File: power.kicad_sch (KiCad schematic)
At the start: 40 parts, among them Q1 DMN3008SFG, Q2 DMN3008SFG, U1 AP33771, U2 AP62150WU, U4 AP62150WU, U5 USBLC6-2SC6

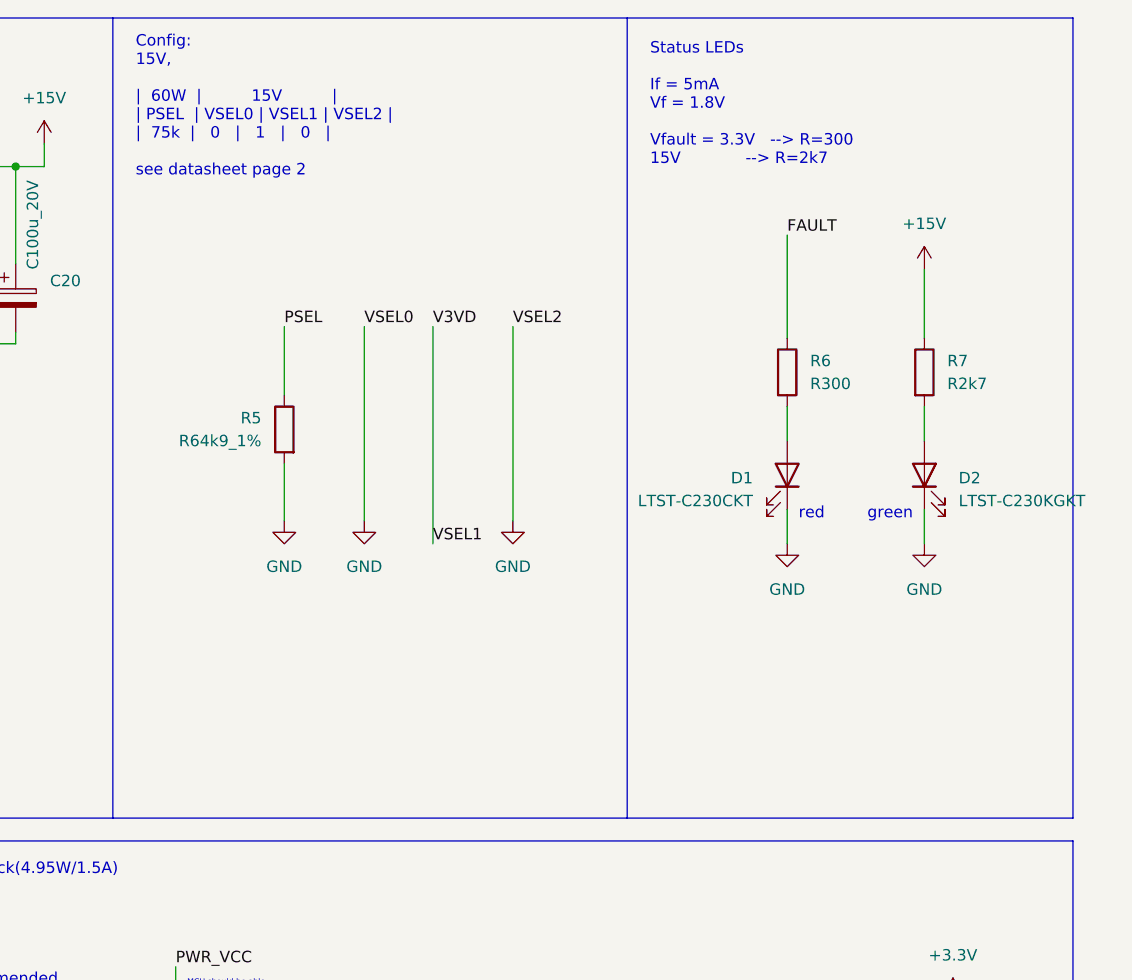
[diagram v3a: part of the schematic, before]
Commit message: Finalize pin mapping, cleanup and layout
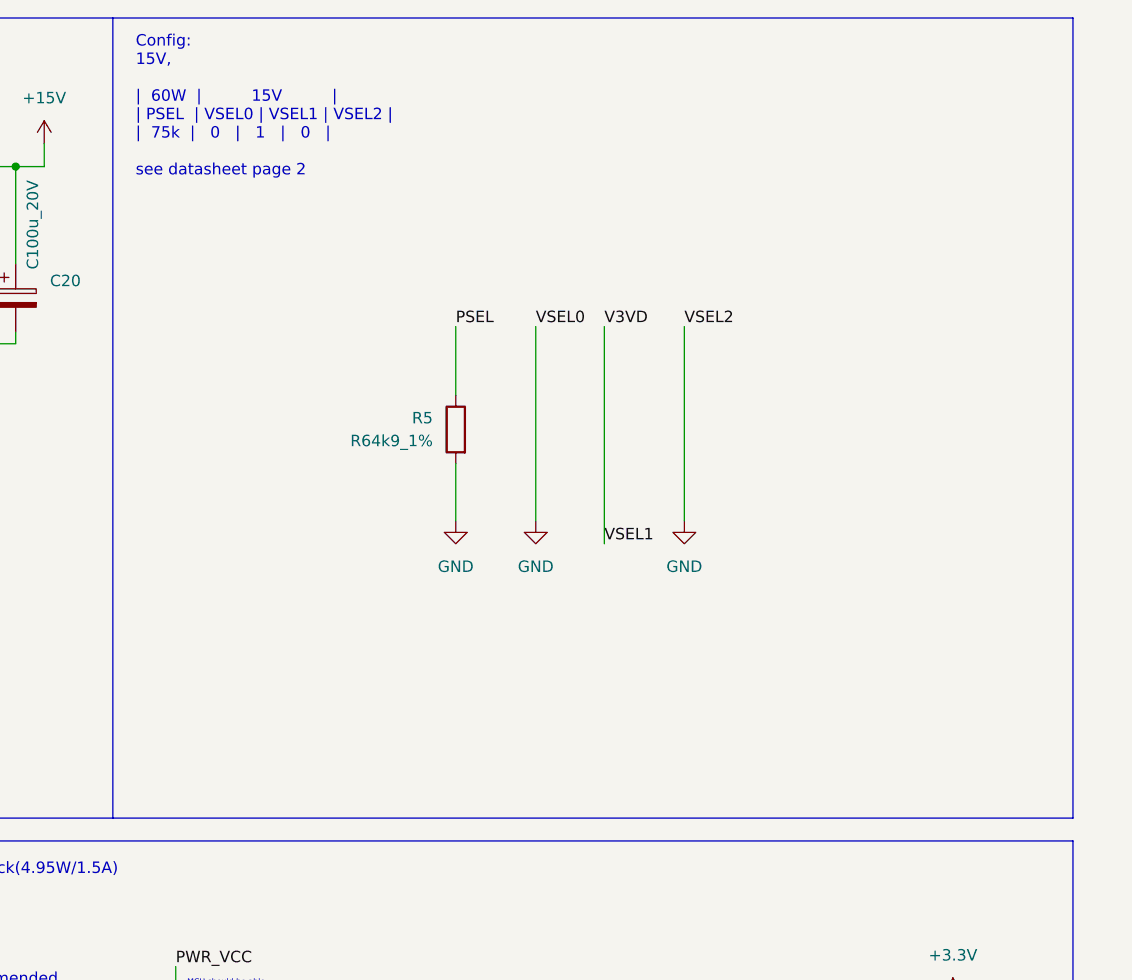
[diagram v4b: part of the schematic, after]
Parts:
- removed D1: LTST-C230CKT, project:LTST-C230, symbol Device:LED
- removed D2: LTST-C230KGKT, project:LTST-C230, symbol Device:LED
- removed R6: R300, Resistor_SMD:R_0805_2012Metric, symbol Device:R
- removed R7: R2k7, Resistor_SMD:R_0805_2012Metric, symbol Device:R
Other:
- note removed: "Status LEDs If = 5mA Vf = 1.8V Vfault = 3.3V --> R=300 15V --> R=2k7"
- note removed: "green"
- note removed: "red"
- moved on the sheet: R5

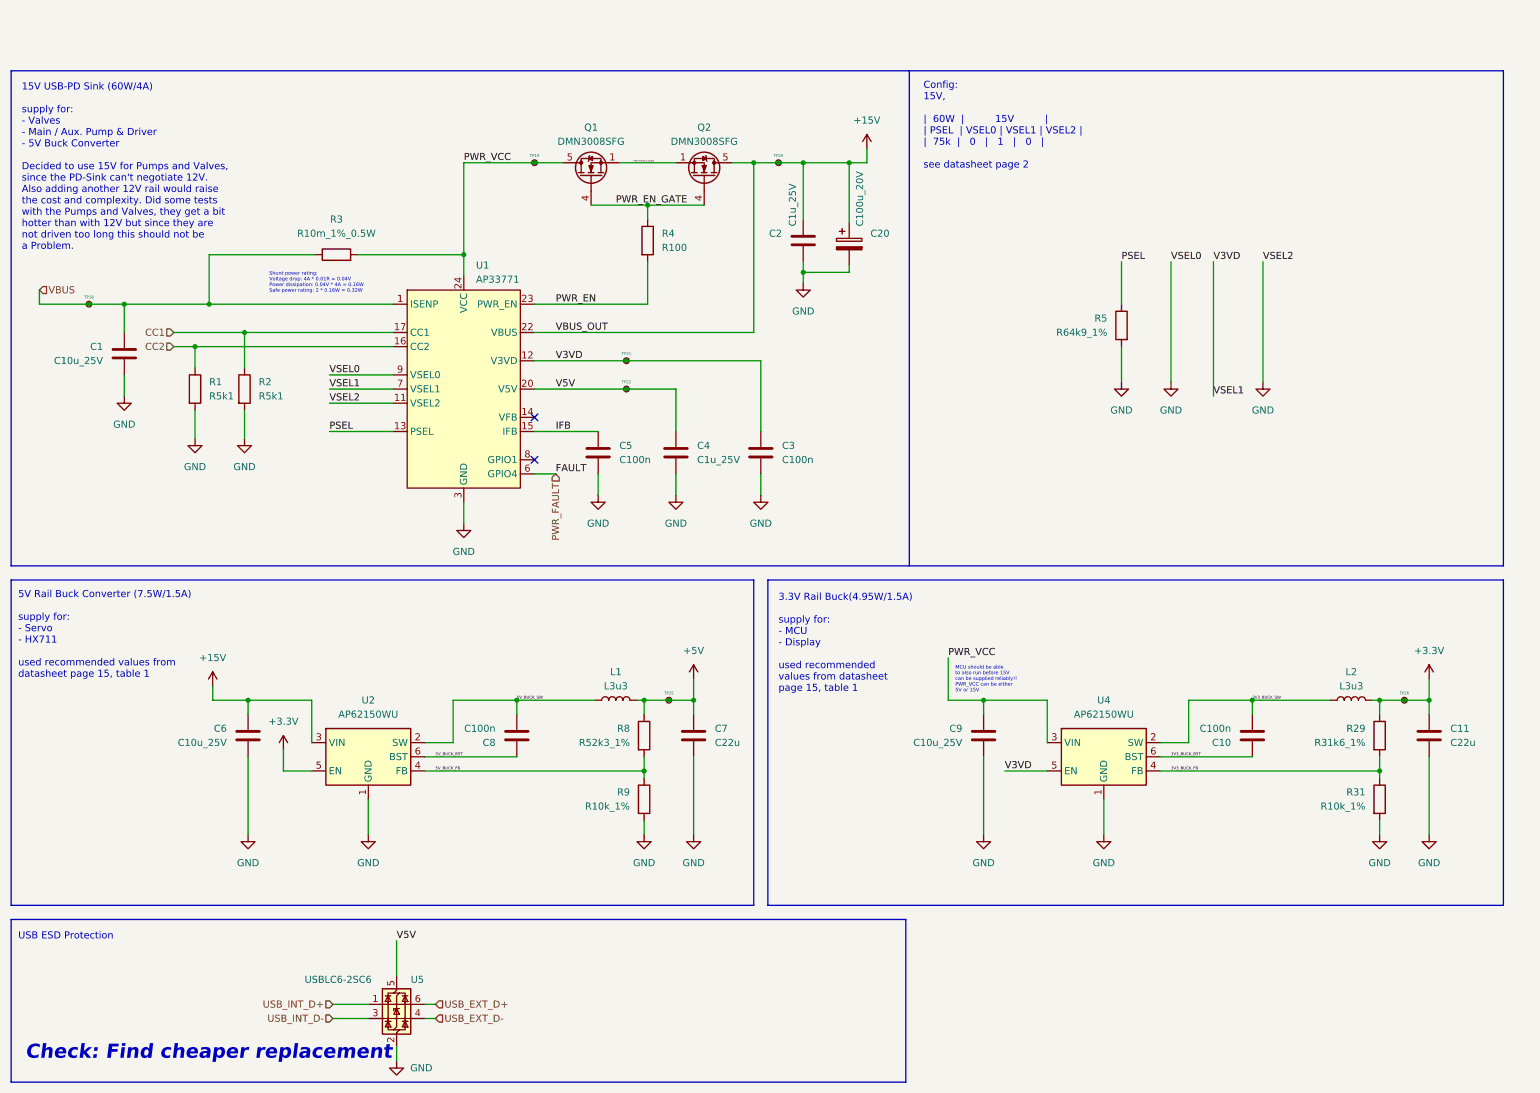
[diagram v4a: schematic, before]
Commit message: Re-annotate parts by board
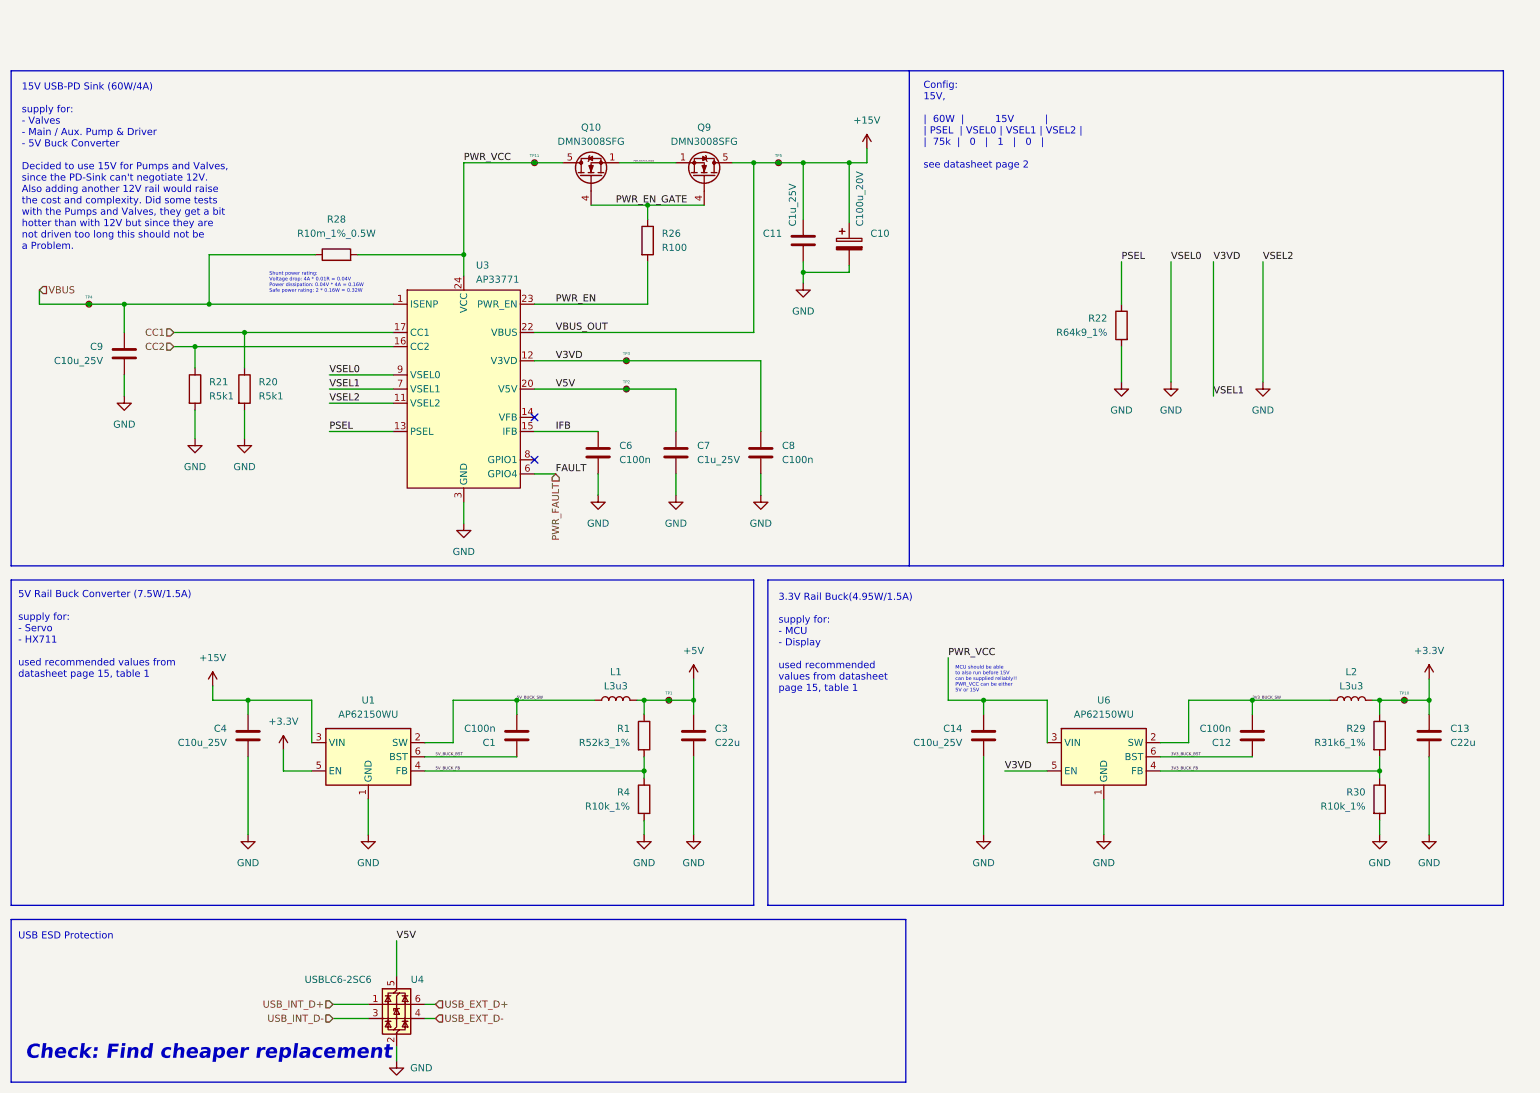
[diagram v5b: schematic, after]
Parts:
- renumbered C8 to C1, C20 to C10, C2 to C11, C10 to C12, C11 to C13, C9 to C14, C7 to C3, C6 to C4, C5 to C6, C4 to C7, C3 to C8, C1 to C9, Q1 to Q10, Q2 to Q9, R8 to R1, R2 to R20, R1 to R21, R5 to R22, R4 to R26, R3 to R28, R31 to R30, R9 to R4, TP25 to TP1, TP26 to TP10, TP19 to TP11, TP22 to TP2, TP21 to TP3, TP18 to TP4, TP20 to TP5, U2 to U1, U1 to U3, U5 to U4, U4 to U6

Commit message: Redesign power rails to use barrel jack 12V input
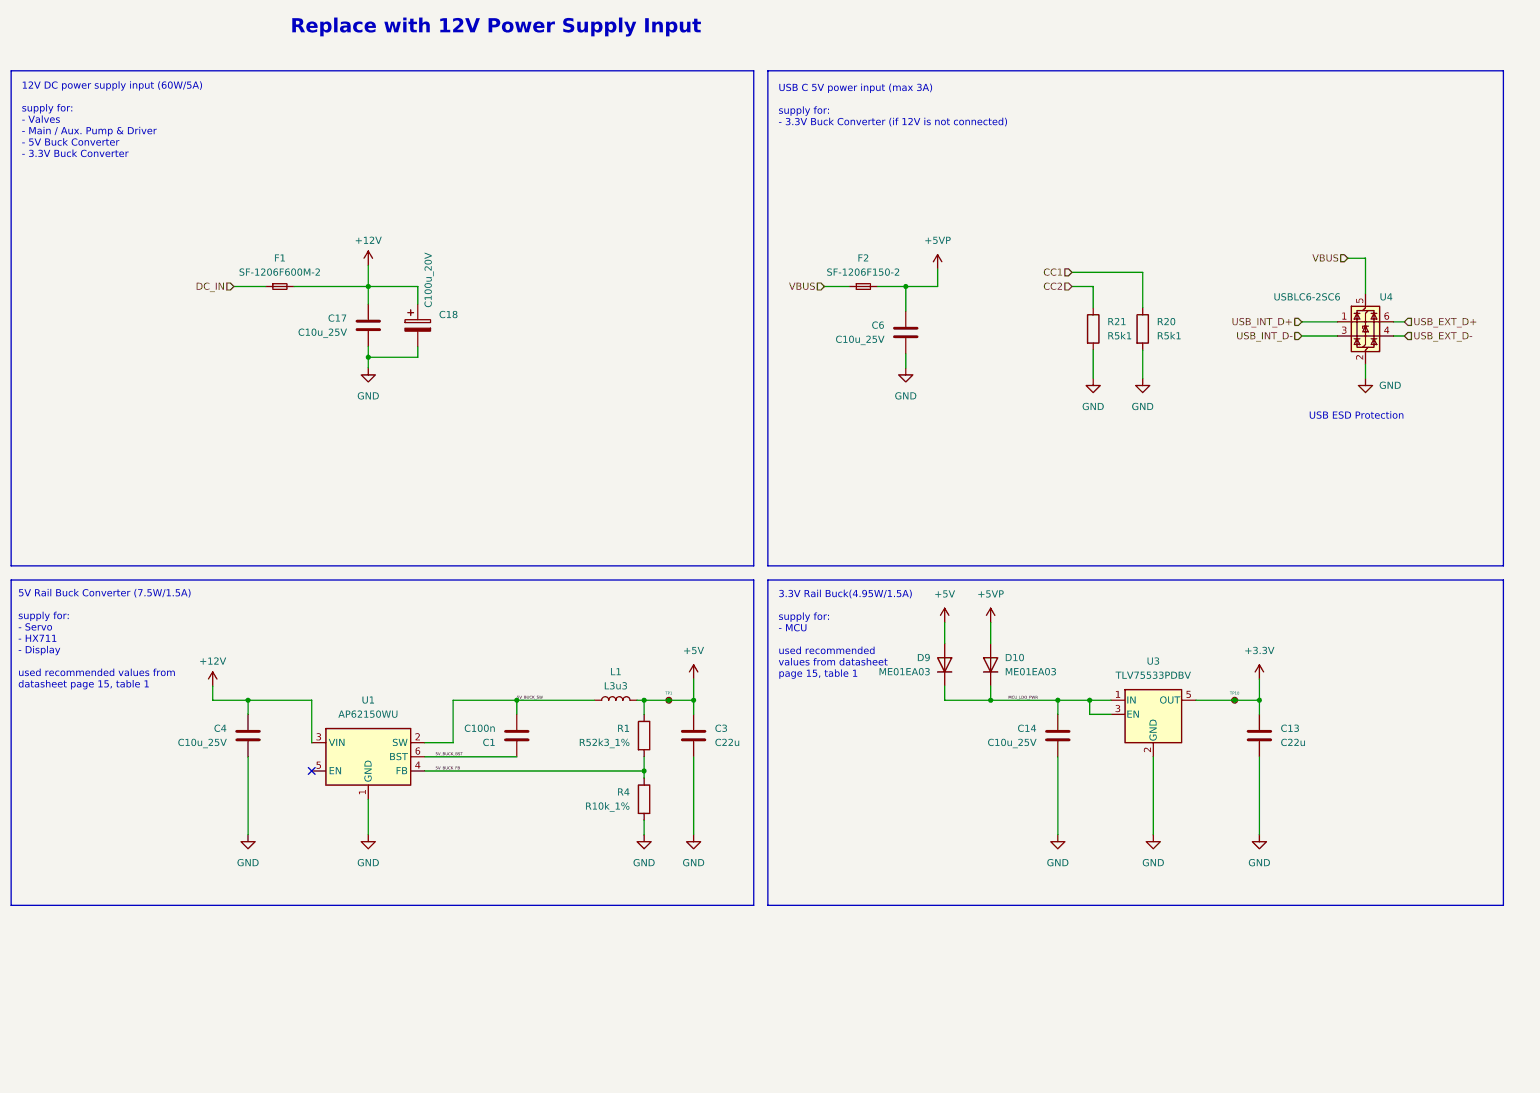
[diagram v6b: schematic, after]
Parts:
- removed C10: C100u_20V, Capacitor_SMD:CP_Elec_6.3x5.9, symbol Device:C_Polarized
- removed C11, C7: C1u_25V, Capacitor_SMD:C_0603_1608Metric, symbol Device:C
- removed C12, C8: C100n, Capacitor_SMD:C_0603_1608Metric, symbol Device:C
- removed C9: C10u_25V, Capacitor_SMD:C_0603_1608Metric, symbol Device:C
- removed L2: L3u3, Inductor_SMD:L_Coilcraft_LPS4018, symbol Device:L
- removed Q10, Q9: DMN3008SFG, Package_SON:Diodes_PowerDI3333-8, symbol Transistor_FET:DMN3008SFG
- removed R22: R64k9_1%, Resistor_SMD:R_0603_1608Metric, symbol Device:R
- removed R26: R100, Resistor_SMD:R_0603_1608Metric, symbol Device:R
- removed R28: R10m_1%_0.5W, Resistor_SMD:R_1206_3216Metric, symbol Device:R
- removed R29: R31k6_1%, Resistor_SMD:R_0805_2012Metric, symbol Device:R
- removed R30: R10k_1%, Resistor_SMD:R_0805_2012Metric, symbol Device:R
- removed TP11, TP2, TP3, TP4, TP5: TestPoint_Small, TestPoint:TestPoint_Pad_D1.5mm, symbol Connector:TestPoint_Small
- removed U3: AP33771, Package_DFN_QFN:QFN-24-1EP_4x4mm_P0.5mm_EP2.7x2.7mm, symbol Interface_USB:AP33771
- removed U6: AP62150WU, Package_TO_SOT_SMD:TSOT-23-6, symbol Regulator_Switching:AP62150WU
- added C17: C10u_25V, Capacitor_SMD:C_0603_1608Metric, symbol Device:C
- added C18: C100u_20V, Capacitor_SMD:CP_Elec_6.3x5.9, symbol Device:C_Polarized
- added D10, D9: ME01EA03, Diode_SMD:D_SOD-128, symbol Device:D
- added F1: SF-1206F600M-2, Fuse:Fuse_1206_3216Metric, symbol Device:Fuse_Small
- added F2: SF-1206F150-2, Fuse:Fuse_1206_3216Metric, symbol Device:Fuse_Small
- added U3: TLV75533PDBV, Package_TO_SOT_SMD:SOT-23-5, symbol Regulator_Linear:TLV75533PDBV
- C6: value C100n -> C10u_25V; Mouser Part Number 80-C0603C104K3R7867 -> 81-GRM188R61E106KA3J
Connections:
- net V5V is gone; now on net VBUS: U4.5 (VBUS)
- net +3.3V: now also U3.5 (OUT); no longer U1.5 (EN)
- net +5V: now also D9.2 (A)
- net GND: now also C17.2, C18.2, U3.2 (GND)
- net VBUS: now also F2.1
- net +15V renamed +12V
- net +12V: now also C17.1, C18.1, F1.2
- net IFB renamed +5VP
- net +5VP: now also D10.2 (A), F2.2
- net PWR_VCC renamed MCU_LDO_PWR
- net MCU_LDO_PWR: now also D10.1 (K), D9.1 (K), U3.1 (IN), U3.3 (EN)
- new net DC_IN: F1.1
- no-connect marks 2 -> 1
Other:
- note added: "12V DC power supply input (60W/5A) supply for: - Valves - Main / Aux. Pump & Driver - 5V Buck Converter - 3.3V Buck Converter"
- note added: "3.3V Rail Buck(4.95W/1.5A) supply for: - MCU used recommended values from datasheet page 15, table 1"
- note added: "5V Rail Buck Converter (7.5W/1.5A) supply for: - Servo - HX711 - Display used recommended values from datasheet page 15, table 1"
- note added: "Replace with 12V Power Supply Input"
- note added: "USB C 5V power input (max 3A) supply for: - 3.3V Buck Converter (if 12V is not connected)"
- note removed: "15V USB-PD Sink (60W/4A) supply for: - Valves - Main / Aux. Pump & Driver - 5V Buck Converter Decided to use 15V for Pumps and Valves, since the PD-Sink can't negotiate 12V. Also adding another 12V rail would raise the cost and complexity. Did some tests with the Pumps and Valves, they get a bit hotter than with 12V but since they are not driven too long this should not be a Problem."
- note removed: "3.3V Rail Buck(4.95W/1.5A) supply for: - MCU - Display used recommended values from datasheet page 15, table 1"
- note removed: "5V Rail Buck Converter (7.5W/1.5A) supply for: - Servo - HX711 used recommended values from datasheet page 15, table 1"
- note removed: "Check: Find cheaper replacement"
- note removed: "Config: 15V, | 60W | 15V | | PSEL | VSEL0 | VSEL1 | VSEL2 | | 75k | 0 | 1 | 0 | see datasheet page 2"
- note removed: "MCU should be able to also run before 15V can be supplied reliably!! PWR_VCC can be either 5V or 15V"
- note removed: "Shunt power rating: Voltage drop: 4A * 0.01R = 0.04V Power dissipation: 0.04V * 4A = 0.16W Safe power rating: 2 * 0.16W = 0.32W"
- moved on the sheet: C13, C14, R20, R21, TP10, U4
